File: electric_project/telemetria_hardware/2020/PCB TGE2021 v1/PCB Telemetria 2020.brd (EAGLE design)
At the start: 160 x 100 mm, 21 parts, among them IC1 INA240A1DR, IC2 MCP3221A6T-E_OTVAO, IC3 AZ1117IH-3.3TRG1, IC4 ACS758LCB-050B-PFF-T

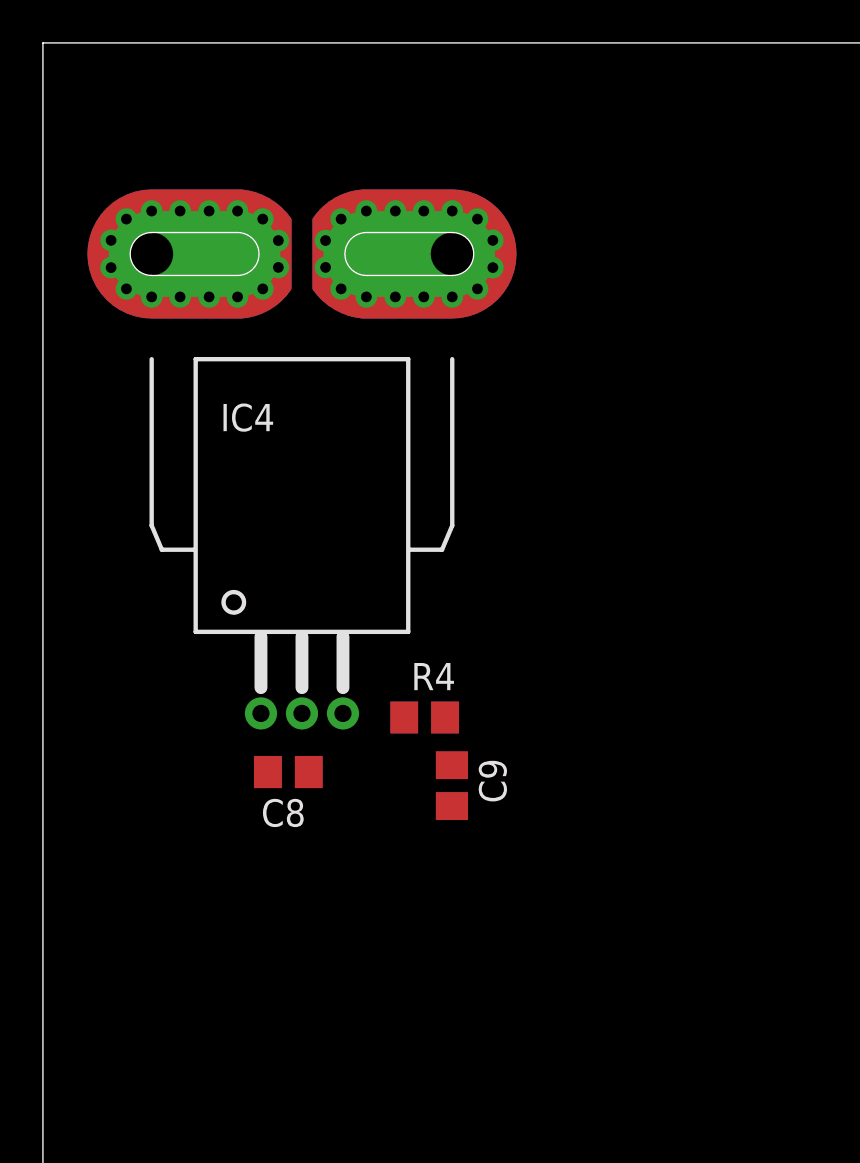
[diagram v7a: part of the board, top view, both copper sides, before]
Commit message: Adding a connector to mppt current sense
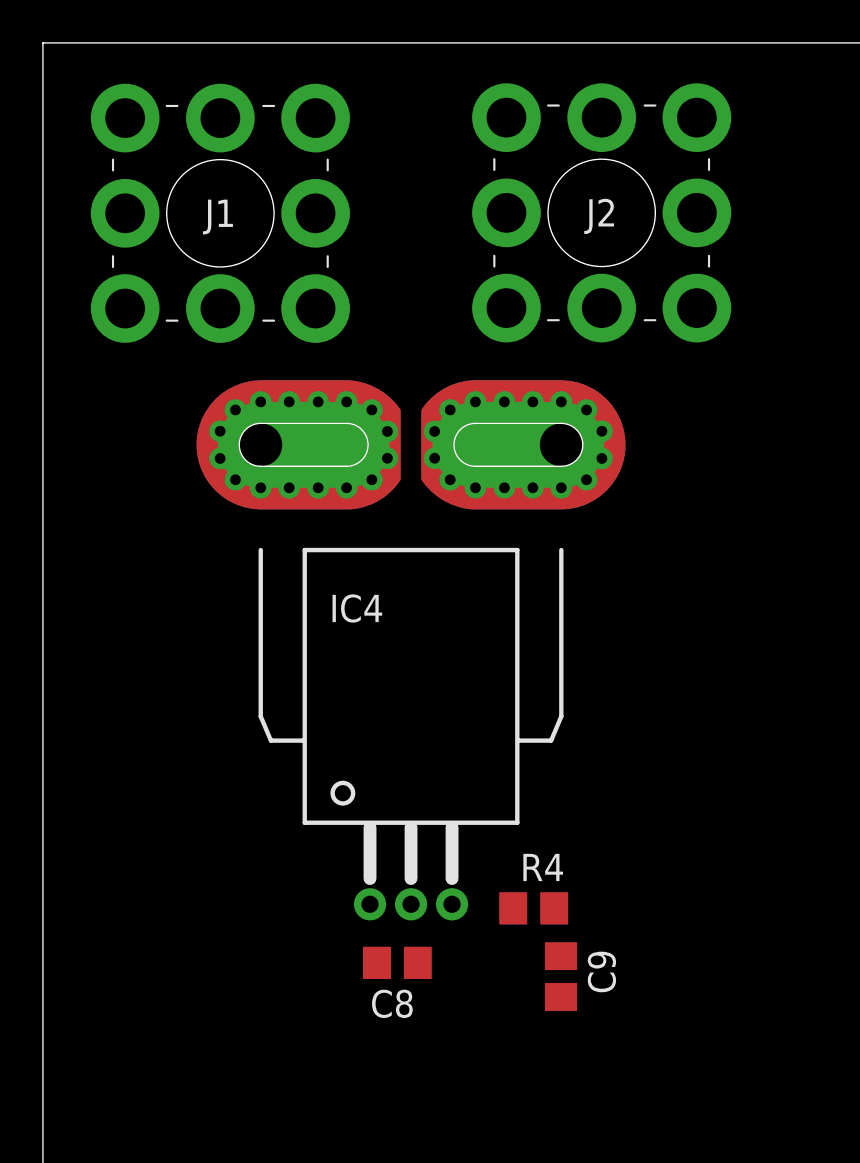
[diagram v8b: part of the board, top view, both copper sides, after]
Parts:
- added J1, J2: 74655095R, SamacSys_Parts:74655095R
- moved C8 10.2 mm to (16.5, 57.1)
- moved C9 10.2 mm to (24.1, 56.5)
- moved IC4 10.2 mm to (17.1, 81.3)
- moved R4 10.2 mm to (22.9, 59.7)
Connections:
- net CMPPT_M: now also J1.1, J1.2, J1.3, J1.4, J1.5, J1.6, J1.7, J1.8
- net CMPPT_P: now also J2.1, J2.2, J2.3, J2.4, J2.5, J2.6, J2.7, J2.8
